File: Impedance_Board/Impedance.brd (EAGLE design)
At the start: 70 x 70 mm, 42 parts, among them IC1 AD8608ARZ, IC2 INA826AID, U4 MC74VHC1GT66DTT1

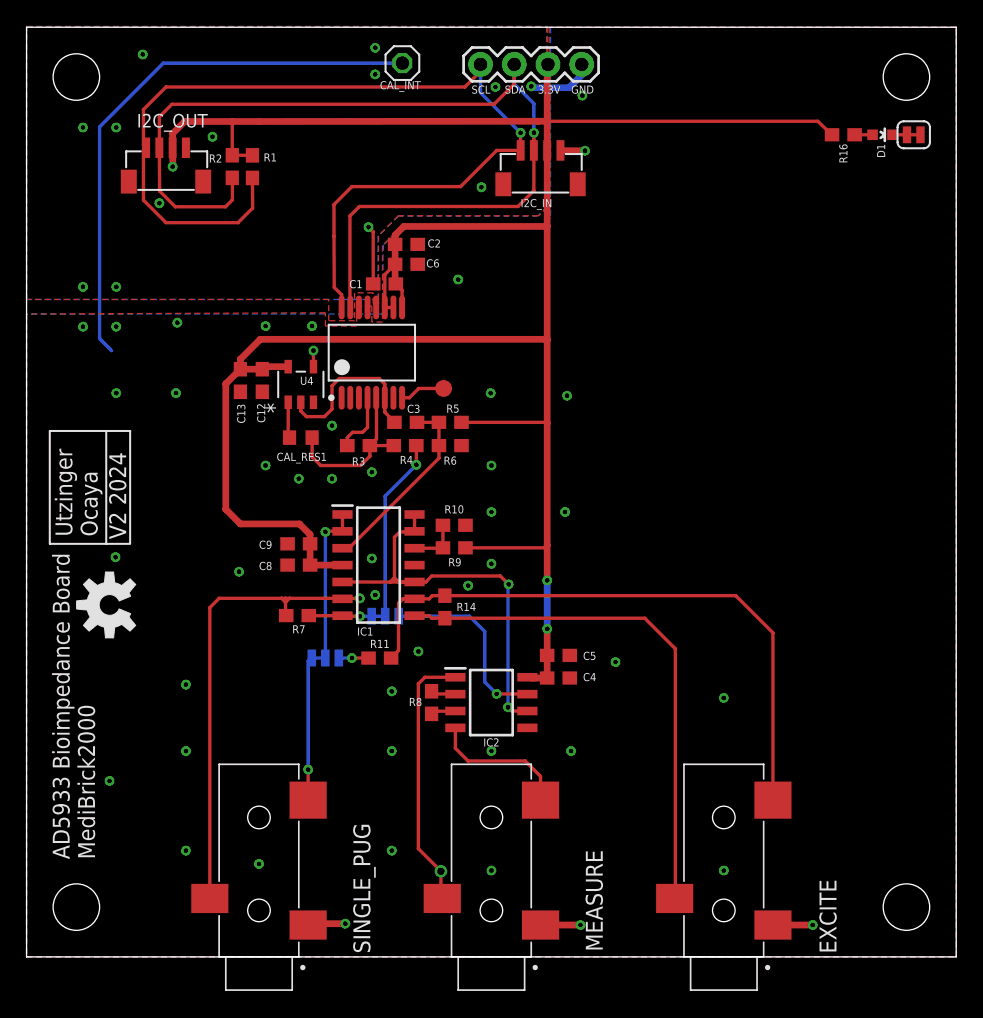
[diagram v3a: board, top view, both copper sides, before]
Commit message: IMU board
Completed IMU board design
Updated designs with ground via close to any other via.
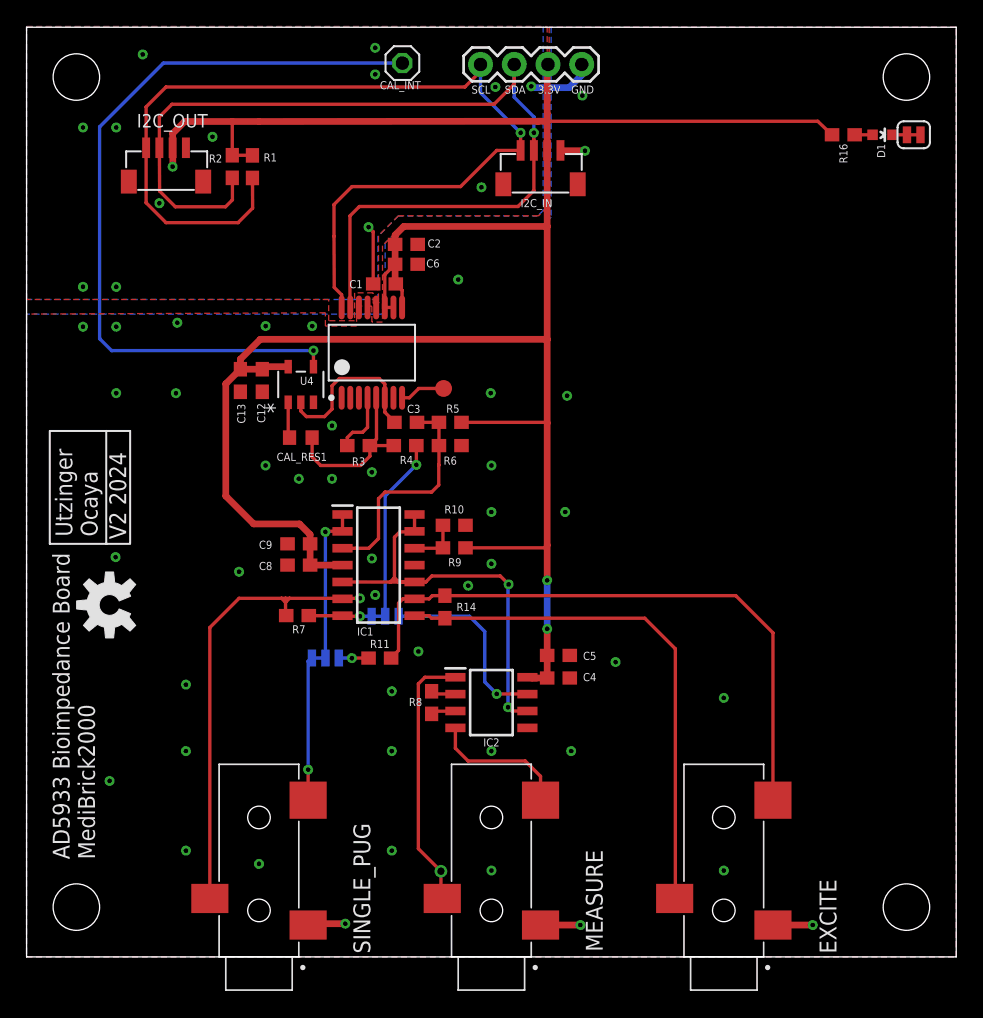
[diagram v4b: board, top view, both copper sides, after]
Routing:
- net N$2: track 43.4 -> 58.6 mm
- net N$6: track 14.4 -> 17.4 mm
- net N$1: track 35.7 -> 34.8 mm
- net 3.3V: track 191.1 -> 190.6 mm
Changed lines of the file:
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@@
 <drawing>
 <settings>
-<setting alwaysvectorfont="no"/>
+<setting alwaysvectorfont="yes"/>
 <setting verticaltext="up"/>
 </settings>
@@
 <vertex x="70" y="0"/>
 <vertex x="70" y="70"/>
-<vertex x="39.45" y="70"/>
-<vertex x="39.45" y="55.65"/>
+<vertex x="39.5" y="70"/>
+<vertex x="39.5" y="55.7"/>
 <vertex x="38.8" y="55"/>
 <vertex x="28.25" y="55"/>
-<vertex x="26.859303125" y="53.609303125"/>
-<vertex x="26.799428125" y="48.4"/>
+<vertex x="27" y="53.76"/>
+<vertex x="27" y="48.4"/>
 </polygon>
 <contactref element="J1" pad="1"/>
@@
 <via x="40.55" y="33.5" extent="1-16" drill="0.35"/>
 <polygon width="0.0762" layer="16" isolate="0.254">
-<vertex x="39.2" y="70.05"/>
-<vertex x="39.2" y="56.5"/>
+<vertex x="38.9" y="70.05"/>
+<vertex x="38.9" y="56.2"/>
 <vertex x="38.5" y="55.8"/>
 <vertex x="28" y="55.8"/>
@@
 <wire x1="37.712" y1="21.055" x2="38" y2="21.055" width="0.254" layer="1"/>
 <wire x1="38" y1="21.055" x2="38.012" y2="21.055" width="0.254" layer="1"/>
-<wire x1="15" y1="43.15" x2="15" y2="33.7" width="0.508" layer="1"/>
-<wire x1="15" y1="33.7" x2="16.1" y2="32.6" width="0.508" layer="1"/>
-<wire x1="16.1" y1="32.6" x2="20.55" y2="32.6" width="0.508" layer="1"/>
+<wire x1="15" y1="43.15" x2="15" y2="34.7" width="0.508" layer="1"/>
+<wire x1="15" y1="34.7" x2="17.1" y2="32.6" width="0.508" layer="1"/>
+<wire x1="17.1" y1="32.6" x2="20.55" y2="32.6" width="0.508" layer="1"/>
 <wire x1="20.55" y1="32.6" x2="21.35" y2="31.8" width="0.508" layer="1"/>
 <wire x1="21.35" y1="31.8" x2="21.35" y2="31.1" width="0.508" layer="1"/>
@@
 <wire x1="23.16711875" y1="50.40788125" x2="23.14826875" y2="54.253246875" width="0.254" layer="1"/>
 <wire x1="15.9236" y1="55.2836" x2="10.5016625" y2="55.2836" width="0.254" layer="1"/>
-<wire x1="8.8006" y1="60.7687625" x2="9" y2="60.924" width="0.254" layer="1"/>
-<wire x1="10.5016625" y1="55.2836" x2="8.8006" y2="56.9846625" width="0.254" layer="1"/>
-<wire x1="8.8006" y1="56.9846625" x2="8.8006" y2="60.7687625" width="0.254" layer="1"/>
-<wire x1="8.8" y1="63.8" x2="8.8" y2="61.124" width="0.254" layer="1"/>
-<wire x1="9" y1="60.924" x2="8.8" y2="61.124" width="0.254" layer="1"/>
+<wire x1="10.5016625" y1="55.2836" x2="9.0006" y2="56.7846625" width="0.254" layer="1"/>
+<wire x1="9" y1="60.924" x2="9.0006" y2="60.9234" width="0.254" layer="1"/>
+<wire x1="9.0006" y1="60.9234" x2="9.0006" y2="56.7846625" width="0.254" layer="1"/>
+<wire x1="9" y1="64" x2="9" y2="60.924" width="0.254" layer="1"/>
 <wire x1="10.5" y1="65.5" x2="33" y2="65.5" width="0.254" layer="1"/>
 <wire x1="34.18" y1="66.68" x2="33" y2="65.5" width="0.254" layer="1"/>
 <wire x1="34.18" y1="66.68" x2="34.18" y2="67.2" width="0.254" layer="1"/>
-<wire x1="8.8" y1="63.8" x2="10.5" y2="65.5" width="0.254" layer="1"/>
+<wire x1="9" y1="64" x2="10.5" y2="65.5" width="0.254" layer="1"/>
 <wire x1="15.9236" y1="55.2836" x2="17.02325625" y2="56.38325625" width="0.254" layer="1"/>
 <wire x1="17.02325625" y1="56.38325625" x2="17.01" y2="58.65" width="0.254" layer="1"/>
@@
 <wire x1="38.2" y1="62.05" x2="38.2" y2="60.9652" width="0.254" layer="1"/>
 <wire x1="38.2" y1="60.9652" x2="38.1794" y2="60.9446" width="0.254" layer="1"/>
-<wire x1="38.2" y1="62.05" x2="38.2" y2="64.25" width="0.254" layer="16"/>
-<wire x1="38.2" y1="64.25" x2="36.72" y2="65.73" width="0.254" layer="16"/>
-<wire x1="36.72" y1="65.73" x2="36.72" y2="67.2" width="0.254" layer="16"/>
+<wire x1="38.2" y1="62.05" x2="38.2" y2="63.25" width="0.254" layer="16"/>
+<wire x1="38.2" y1="63.25" x2="36.72" y2="64.73" width="0.254" layer="16"/>
+<wire x1="36.72" y1="64.73" x2="36.72" y2="67.2" width="0.254" layer="16"/>
 <wire x1="24.35" y1="55.79280625" x2="25.05719375" y2="56.5" width="0.254" layer="1"/>
 <wire x1="37" y1="56.5" x2="38.2" y2="57.7" width="0.254" layer="1"/>
@@
 <wire x1="10.3" y1="67.3" x2="5.5" y2="62.5" width="0.254" layer="16"/>
 <wire x1="5.5" y1="62.5" x2="5.5" y2="46.55" width="0.254" layer="16"/>
-<wire x1="6.4" y1="45.65" x2="5.5" y2="46.55" width="0.254" layer="16"/>
+<wire x1="5.5" y1="46.55" x2="6.4" y2="45.65" width="0.254" layer="16"/>
 <wire x1="21.6" y1="44.43985" x2="21.6" y2="45.65" width="0.254" layer="1"/>
 <wire x1="21.6" y1="45.65" x2="21.600015625" y2="45.649984375" width="0.254" layer="1"/>
 <wire x1="21.600015625" y1="45.649984375" x2="21.600015625" y2="45.439834375" width="0.254" layer="1"/>
 <via x="21.6" y="45.65" extent="1-16" drill="0.35"/>
-<wire x1="6.4" y1="45.65" x2="21.600015625" y2="45.439834375" width="0" layer="19" extent="1-16"/>
+<wire x1="6.4" y1="45.65" x2="21.6" y2="45.65" width="0.254" layer="16"/>
 </signal>
 <signal name="N$24">
@@
 <contactref element="R5" pad="2"/>
 <contactref element="IC1" pad="3"/>
-<wire x1="24.2674625" y1="30.7674625" x2="23.788871875" y2="30.769128125" width="0.254" layer="1"/>
+<wire x1="31.05" y1="37.035928125" x2="31.05" y2="38.5" width="0.254" layer="1"/>
+<wire x1="26.5" y1="31.5" x2="25.76575625" y2="30.76575625" width="0.254" layer="1"/>
+<wire x1="25.76575625" y1="30.76575625" x2="24.75796875" y2="30.76575625" width="0.254" layer="1"/>
+<wire x1="24.75796875" y1="30.76575625" x2="23.788871875" y2="30.769128125" width="0.254" layer="1"/>
 <wire x1="23.788" y1="30.77" x2="23.788871875" y2="30.769128125" width="0.254" layer="1"/>
 <wire x1="31.05" y1="40.25" x2="31.05" y2="38.5" width="0.254" layer="1"/>
-<wire x1="31.05" y1="38.5" x2="31.05" y2="37.55" width="0.254" layer="1"/>
-<wire x1="31.05" y1="37.55" x2="24.2674625" y2="30.7674625" width="0.254" layer="1"/>
 <wire x1="31.05" y1="40.25" x2="29.4" y2="40.25" width="0.254" layer="1"/>
+<wire x1="26.5" y1="31.5" x2="26.5" y2="34.5" width="0.254" layer="1"/>
+<wire x1="26.5" y1="34.5" x2="27" y2="35" width="0.254" layer="1"/>
+<wire x1="27" y1="35" x2="30.5" y2="35" width="0.254" layer="1"/>
+<wire x1="30.5" y1="35" x2="31.035928125" y2="35.535928125" width="0.254" layer="1"/>
+<wire x1="31.035928125" y1="35.535928125" x2="31.035928125" y2="37.035928125" width="0.254" layer="1"/>
+<wire x1="31.035928125" y1="37.035928125" x2="31.05" y2="37.035928125" width="0.254" layer="1"/>
 </signal>
 <signal name="N$9">
@@
 <contactref element="IC1" pad="6"/>
 <contactref element="R7" pad="1"/>
-<wire x1="13.8" y1="4.4" x2="13.8" y2="26.3" width="0.254" layer="1"/>
-<wire x1="13.8" y1="26.3" x2="14.5" y2="27" width="0.254" layer="1"/>
-<wire x1="14.5" y1="27" x2="19.2" y2="27" width="0.254" layer="1"/>
+<wire x1="13.8" y1="4.4" x2="13.8" y2="24.8" width="0.254" layer="1"/>
+<wire x1="13.8" y1="24.8" x2="16" y2="27" width="0.254" layer="1"/>
+<wire x1="16" y1="27" x2="19.2" y2="27" width="0.254" layer="1"/>
 <wire x1="19.2" y1="27" x2="19.5" y2="27" width="0.254" layer="1"/>
 <wire x1="19.5" y1="27" x2="19.8" y2="27" width="0.254" layer="1"/>
